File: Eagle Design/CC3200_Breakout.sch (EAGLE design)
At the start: 46 parts, among them J22 M10X2, J23 M10X2, U15 AT25FS010, Y2 32.768KHz, Y3 407MHz

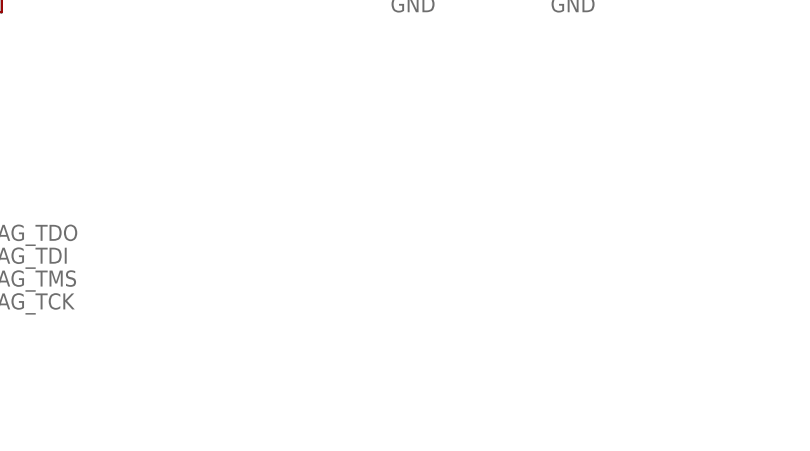
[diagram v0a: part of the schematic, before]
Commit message: Added JTAG and Lock Connectors
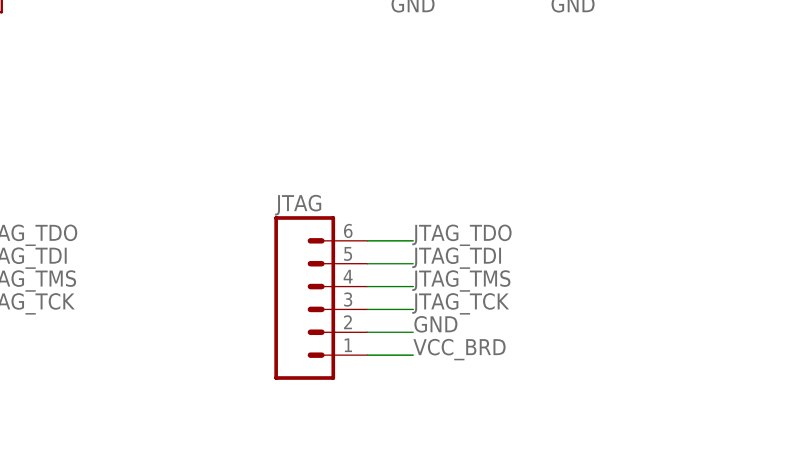
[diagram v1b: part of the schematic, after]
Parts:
- added JTAG: (no value), SparkFun-Connectors:M06SILK_FEMALE_PTH
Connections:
- net GND: now also JTAG.2
- net JTAG_TCK: now also JTAG.3
- net JTAG_TDI: now also JTAG.5
- net JTAG_TDO: now also JTAG.6
- net JTAG_TMS: now also JTAG.4
- net VCC_BRD: now also JTAG.1
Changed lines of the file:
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@@
 <?xml version="1.0" encoding="utf-8"?>
 <!DOCTYPE eagle SYSTEM "eagle.dtd">
-<eagle version="6.4">
+<eagle version="7.1.0">
 <drawing>
 <settings>
@@
 <layers>
 <layer number="1" name="Top" color="4" fill="1" visible="no" active="no"/>
+<layer number="2" name="Route2" color="1" fill="3" visible="no" active="no"/>
+<layer number="3" name="Route3" color="4" fill="3" visible="no" active="no"/>
+<layer number="14" name="Route14" color="1" fill="6" visible="no" active="no"/>
+<layer number="15" name="Route15" color="4" fill="6" visible="no" active="no"/>
 <layer number="16" name="Bottom" color="1" fill="1" visible="no" active="no"/>
 <layer number="17" name="Pads" color="2" fill="1" visible="no" active="no"/>
@@
 <layer number="54" name="bGND_GNDA" color="1" fill="9" visible="no" active="no"/>
 <layer number="56" name="wert" color="7" fill="1" visible="no" active="no"/>
+<layer number="57" name="tCAD" color="7" fill="1" visible="no" active="no"/>
+<layer number="90" name="Modules" color="5" fill="1" visible="yes" active="yes"/>
 <layer number="91" name="Nets" color="2" fill="1" visible="yes" active="yes"/>
 <layer number="92" name="Busses" color="1" fill="1" visible="yes" active="yes"/>
@@
 <layer number="97" name="Info" color="7" fill="1" visible="yes" active="yes"/>
 <layer number="98" name="Guide" color="6" fill="1" visible="yes" active="yes"/>
+<layer number="99" name="SpiceOrder" color="7" fill="1" visible="yes" active="yes"/>
 <layer number="100" name="Muster" color="7" fill="1" visible="no" active="no"/>
 <layer number="101" name="Patch_Top" color="12" fill="4" visible="no" active="yes"/>
@@
 <layer number="108" name="tplace-old" color="10" fill="1" visible="yes" active="yes"/>
 <layer number="109" name="ref-old" color="11" fill="1" visible="yes" active="yes"/>
+<layer number="110" name="fp0" color="7" fill="1" visible="yes" active="yes"/>
+<layer number="111" name="LPC17xx" color="7" fill="1" visible="yes" active="yes"/>
+<layer number="112" name="tSilk" color="7" fill="1" visible="yes" active="yes"/>
+<layer number="113" name="IDFDebug" color="4" fill="1" visible="yes" active="yes"/>
 <layer number="116" name="Patch_BOT" color="9" fill="4" visible="no" active="yes"/>
 <layer number="121" name="_tsilk" color="7" fill="1" visible="no" active="yes"/>
 <layer number="122" name="_bsilk" color="7" fill="1" visible="no" active="yes"/>
+<layer number="123" name="tTestmark" color="7" fill="1" visible="yes" active="yes"/>
+<layer number="124" name="bTestmark" color="7" fill="1" visible="yes" active="yes"/>
 <layer number="125" name="_tNames" color="7" fill="1" visible="no" active="yes"/>
+<layer number="126" name="_bNames" color="7" fill="1" visible="yes" active="yes"/>
+<layer number="127" name="_tValues" color="7" fill="1" visible="yes" active="yes"/>
+<layer number="128" name="_bValues" color="7" fill="1" visible="yes" active="yes"/>
+<layer number="131" name="tAdjust" color="7" fill="1" visible="yes" active="yes"/>
+<layer number="132" name="bAdjust" color="7" fill="1" visible="yes" active="yes"/>
 <layer number="144" name="Drill_legend" color="7" fill="1" visible="no" active="yes"/>
+<layer number="150" name="Notes" color="7" fill="1" visible="yes" active="yes"/>
 <layer number="151" name="HeatSink" color="7" fill="1" visible="no" active="yes"/>
+<layer number="152" name="_bDocu" color="7" fill="1" visible="yes" active="yes"/>
+<layer number="153" name="FabDoc1" color="7" fill="1" visible="yes" active="yes"/>
+<layer number="154" name="FabDoc2" color="7" fill="1" visible="yes" active="yes"/>
+<layer number="155" name="FabDoc3" color="7" fill="1" visible="yes" active="yes"/>
 <layer number="199" name="Contour" color="7" fill="1" visible="no" active="yes"/>
 <layer number="200" name="200bmp" color="1" fill="10" visible="no" active="yes"/>
@@
 <layer number="223" name="223bmp" color="24" fill="1" visible="no" active="no"/>
 <layer number="224" name="224bmp" color="25" fill="1" visible="no" active="no"/>
+<layer number="248" name="Housing" color="7" fill="1" visible="yes" active="yes"/>
+<layer number="249" name="Edge" color="7" fill="1" visible="yes" active="yes"/>
 <layer number="250" name="Descript" color="3" fill="1" visible="no" active="no"/>
 <layer number="251" name="SMDround" color="12" fill="11" visible="no" active="no"/>
@@
 <part name="J22" library="SparkFun-Connectors" deviceset="M10X2" device=""/>
 <part name="J23" library="SparkFun-Connectors" deviceset="M10X2" device=""/>
+<part name="JTAG" library="SparkFun-Connectors" deviceset="M06" device="SILK_FEMALE_PTH"/>
 </parts>
 <sheets>
@@
 <instance part="J22" gate="G$1" x="210.82" y="132.08"/>
 <instance part="J23" gate="G$1" x="271.78" y="132.08"/>
+<instance part="JTAG" gate="G$1" x="193.04" y="25.4"/>
 </instances>
 <busses>
@@
 <label x="154.94" y="33.02" size="1.778" layer="95"/>
 </segment>
+<segment>
+<wire x1="198.12" y1="33.02" x2="203.2" y2="33.02" width="0.1524" layer="91"/>
+<label x="203.2" y="33.02" size="1.778" layer="95"/>
+<pinref part="JTAG" gate="G$1" pin="6"/>
+</segment>
 </net>
 <net name="JTAG_TDI" class="0">
@@
 <label x="154.94" y="30.48" size="1.778" layer="95"/>
 </segment>
+<segment>
+<wire x1="198.12" y1="30.48" x2="203.2" y2="30.48" width="0.1524" layer="91"/>
+<label x="203.2" y="30.48" size="1.778" layer="95"/>
+<pinref part="JTAG" gate="G$1" pin="5"/>
+</segment>
 </net>
 <net name="JTAG_TMS" class="0">
@@
 <label x="154.94" y="27.94" size="1.778" layer="95"/>
 </segment>
+<segment>
+<wire x1="198.12" y1="27.94" x2="203.2" y2="27.94" width="0.1524" layer="91"/>
+<label x="203.2" y="27.94" size="1.778" layer="95"/>
+<pinref part="JTAG" gate="G$1" pin="4"/>
+</segment>
 </net>
 <net name="JTAG_TCK" class="0">
@@
 <wire x1="116.84" y1="25.4" x2="116.84" y2="53.34" width="0.1524" layer="91"/>
 <label x="154.94" y="25.4" size="1.778" layer="95"/>
+</segment>
+<segment>
+<wire x1="198.12" y1="25.4" x2="203.2" y2="25.4" width="0.1524" layer="91"/>
+<label x="203.2" y="25.4" size="1.778" layer="95"/>
+<pinref part="JTAG" gate="G$1" pin="3"/>
 </segment>
 </net>
@@
 <wire x1="289.56" y1="142.24" x2="279.4" y2="142.24" width="0.1524" layer="91"/>
 <label x="289.56" y="142.24" size="1.778" layer="95"/>
+</segment>
+<segment>
+<wire x1="198.12" y1="22.86" x2="203.2" y2="22.86" width="0.1524" layer="91"/>
+<label x="203.2" y="22.86" size="1.778" layer="95"/>
+<pinref part="JTAG" gate="G$1" pin="2"/>
 </segment>
 </net>
@@
 <label x="193.04" y="142.24" size="1.778" layer="95"/>
 </segment>
-</net>
+<segment>
+<pinref part="JTAG" gate="G$1" pin="1"/>
+<wire x1="198.12" y1="20.32" x2="203.2" y2="20.32" width="0.1524" layer="91"/>
+<label x="203.2" y="20.32" size="1.778" layer="95"/>
+</segment>
+</net>

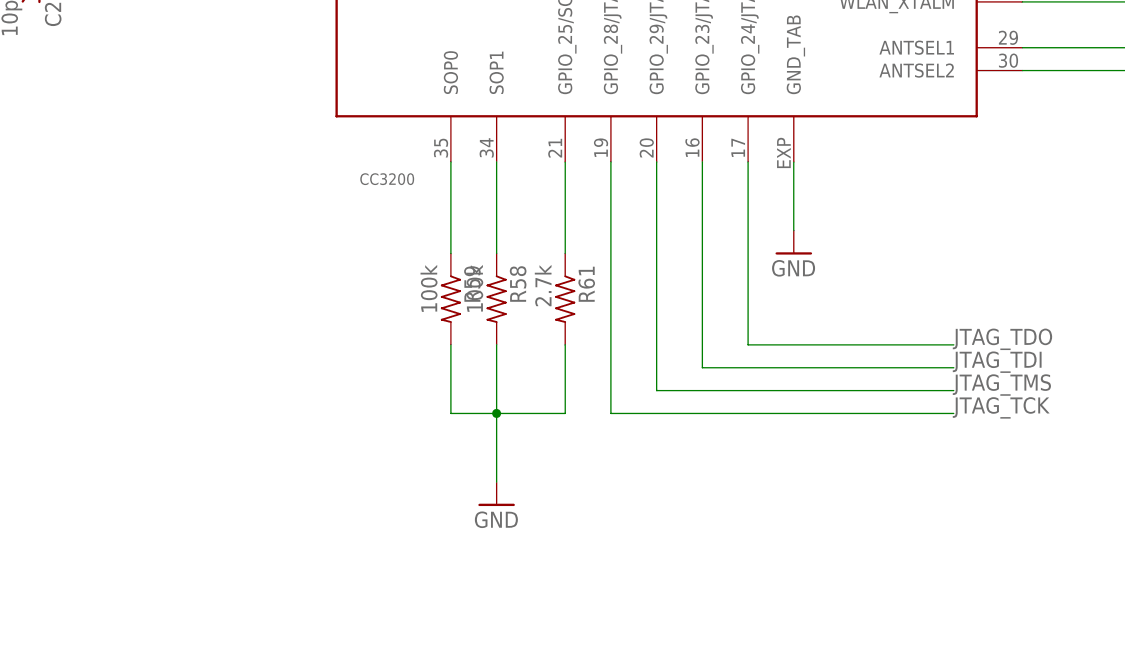
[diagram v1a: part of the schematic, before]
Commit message: SOP
Added SOP connector and addition connector JP90 to be use as jumper wire
used in Energia
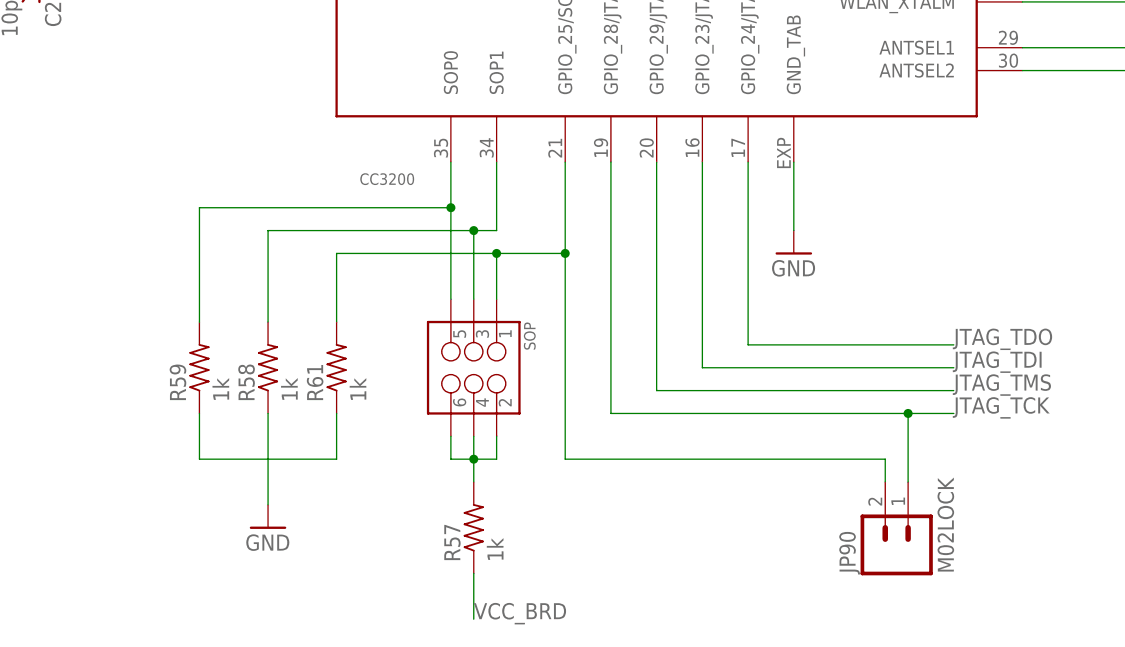
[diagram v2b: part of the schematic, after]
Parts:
- added JP90: M02LOCK, SparkFun-Connectors:M02LOCK
- added R57: 1k, resistor:R-US_R0402
- added SOP: (no value), SparkFun-Connectors:M03X22X3_SILK_MALE_PTH
- R58, R59: value 100k -> 1k
- R61: value 2.7k -> 1k
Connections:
- new net N$6: R57.2, SOP.2, SOP.4, SOP.6
- net GND: now also R58.1, R59.1, R61.1; no longer R58.2, R59.2, R61.2
- net JTAG_TCK: now also JP90.1
- net N$13: now also R59.2, SOP.5; no longer R59.1
- net N$21: now also R58.2, SOP.3; no longer R58.1
- net N$22: now also JP90.2, R61.2, SOP.1; no longer R61.1
- net VCC_BRD: now also R57.1
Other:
- moved on the sheet: R58, R59, R61
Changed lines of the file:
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@@
 <part name="R65" library="resistor" deviceset="R-US_" device="R0402"/>
 <part name="Y2" library="SparkFun-FreqCtrl" deviceset="CRYSTAL" device="5X3" value="32.768KHz"/>
-<part name="R58" library="resistor" deviceset="R-US_" device="R0402" value="100k"/>
-<part name="R61" library="resistor" deviceset="R-US_" device="R0402" value="2.7k"/>
-<part name="R59" library="resistor" deviceset="R-US_" device="R0402" value="100k"/>
-<part name="GND25" library="SparkFun-Aesthetics" deviceset="GND" device=""/>
 <part name="GND23" library="SparkFun-Aesthetics" deviceset="GND" device=""/>
 <part name="GND13" library="SparkFun-Aesthetics" deviceset="GND" device=""/>
@@
 <part name="J23" library="SparkFun-Connectors" deviceset="M10X2" device=""/>
 <part name="JTAG" library="SparkFun-Connectors" deviceset="M06" device="SILK_FEMALE_PTH"/>
+<part name="SOP" library="SparkFun-Connectors" deviceset="M03X2" device="2X3_SILK_MALE_PTH"/>
+<part name="R57" library="resistor" deviceset="R-US_" device="R0402" value="1k"/>
+<part name="JP90" library="SparkFun-Connectors" deviceset="M02" device="LOCK"/>
+<part name="R59" library="resistor" deviceset="R-US_" device="R0402" value="1k"/>
+<part name="R58" library="resistor" deviceset="R-US_" device="R0402" value="1k"/>
+<part name="R61" library="resistor" deviceset="R-US_" device="R0402" value="1k"/>
+<part name="GND25" library="SparkFun-Aesthetics" deviceset="GND" device=""/>
 </parts>
 <sheets>
@@
 <instance part="R65" gate="G$1" x="27.94" y="106.68" rot="R180"/>
 <instance part="Y2" gate="G$1" x="60.96" y="78.74" rot="R90"/>
-<instance part="R58" gate="G$1" x="104.14" y="38.1" rot="R270"/>
-<instance part="R61" gate="G$1" x="111.76" y="38.1" rot="R270"/>
-<instance part="R59" gate="G$1" x="99.06" y="38.1" rot="R270"/>
-<instance part="GND25" gate="1" x="104.14" y="15.24"/>
 <instance part="GND23" gate="1" x="137.16" y="43.18"/>
 <instance part="GND13" gate="1" x="43.18" y="83.82" rot="R270"/>
@@
 <instance part="J23" gate="G$1" x="271.78" y="132.08"/>
 <instance part="JTAG" gate="G$1" x="193.04" y="25.4"/>
+<instance part="SOP" gate="G$1" x="101.6" y="30.48" rot="R270"/>
+<instance part="R57" gate="G$1" x="101.6" y="12.7" rot="R90"/>
+<instance part="JP90" gate="G$1" x="149.86" y="10.16" rot="R90"/>
+<instance part="R59" gate="G$1" x="71.12" y="30.48" rot="R90"/>
+<instance part="R58" gate="G$1" x="78.74" y="30.48" rot="R90"/>
+<instance part="R61" gate="G$1" x="86.36" y="30.48" rot="R90"/>
+<instance part="GND25" gate="1" x="78.74" y="12.7"/>
 </instances>
 <busses>
@@
 <net name="N$13" class="0">
 <segment>
-<pinref part="R59" gate="G$1" pin="1"/>
 <pinref part="U$1" gate="G$1" pin="SOP0"/>
-<wire x1="99.06" y1="43.18" x2="99.06" y2="53.34" width="0.1524" layer="91"/>
+<wire x1="99.06" y1="38.1" x2="99.06" y2="48.26" width="0.1524" layer="91"/>
+<pinref part="SOP" gate="G$1" pin="5"/>
+<pinref part="R59" gate="G$1" pin="2"/>
+<wire x1="99.06" y1="48.26" x2="99.06" y2="53.34" width="0.1524" layer="91"/>
+<wire x1="99.06" y1="48.26" x2="71.12" y2="48.26" width="0.1524" layer="91"/>
+<wire x1="71.12" y1="48.26" x2="71.12" y2="35.56" width="0.1524" layer="91"/>
+<junction x="99.06" y="48.26"/>
 </segment>
 </net>
@@
 <segment>
 <pinref part="U$1" gate="G$1" pin="SOP1"/>
-<pinref part="R58" gate="G$1" pin="1"/>
-<wire x1="104.14" y1="53.34" x2="104.14" y2="43.18" width="0.1524" layer="91"/>
+<wire x1="104.14" y1="53.34" x2="104.14" y2="45.72" width="0.1524" layer="91"/>
+<pinref part="SOP" gate="G$1" pin="3"/>
+<wire x1="104.14" y1="45.72" x2="101.6" y2="45.72" width="0.1524" layer="91"/>
+<wire x1="101.6" y1="45.72" x2="101.6" y2="38.1" width="0.1524" layer="91"/>
+<pinref part="R58" gate="G$1" pin="2"/>
+<wire x1="101.6" y1="45.72" x2="78.74" y2="45.72" width="0.1524" layer="91"/>
+<wire x1="78.74" y1="45.72" x2="78.74" y2="35.56" width="0.1524" layer="91"/>
+<junction x="101.6" y="45.72"/>
 </segment>
 </net>
@@
 <segment>
 <pinref part="U$1" gate="G$1" pin="GPIO_25/SOP2"/>
-<pinref part="R61" gate="G$1" pin="1"/>
 <wire x1="111.76" y1="53.34" x2="111.76" y2="43.18" width="0.1524" layer="91"/>
+<pinref part="JP90" gate="G$1" pin="2"/>
+<wire x1="111.76" y1="43.18" x2="111.76" y2="20.32" width="0.1524" layer="91"/>
+<wire x1="111.76" y1="20.32" x2="147.32" y2="20.32" width="0.1524" layer="91"/>
+<wire x1="147.32" y1="20.32" x2="147.32" y2="17.78" width="0.1524" layer="91"/>
+<pinref part="SOP" gate="G$1" pin="1"/>
+<wire x1="111.76" y1="43.18" x2="104.14" y2="43.18" width="0.1524" layer="91"/>
+<wire x1="104.14" y1="43.18" x2="104.14" y2="38.1" width="0.1524" layer="91"/>
+<pinref part="R61" gate="G$1" pin="2"/>
+<wire x1="104.14" y1="43.18" x2="86.36" y2="43.18" width="0.1524" layer="91"/>
+<wire x1="86.36" y1="43.18" x2="86.36" y2="35.56" width="0.1524" layer="91"/>
+<junction x="104.14" y="43.18"/>
+<junction x="111.76" y="43.18"/>
 </segment>
 </net>
@@
 <segment>
 <pinref part="U$1" gate="G$1" pin="GPIO_28/JTAG_TCK"/>
-<wire x1="154.94" y1="25.4" x2="116.84" y2="25.4" width="0.1524" layer="91"/>
+<wire x1="154.94" y1="25.4" x2="149.86" y2="25.4" width="0.1524" layer="91"/>
+<wire x1="149.86" y1="25.4" x2="116.84" y2="25.4" width="0.1524" layer="91"/>
 <wire x1="116.84" y1="25.4" x2="116.84" y2="53.34" width="0.1524" layer="91"/>
 <label x="154.94" y="25.4" size="1.778" layer="95"/>
+<pinref part="JP90" gate="G$1" pin="1"/>
+<wire x1="149.86" y1="17.78" x2="149.86" y2="25.4" width="0.1524" layer="91"/>
+<junction x="149.86" y="25.4"/>
 </segment>
 <segment>
@@
 </net>
 <net name="GND" class="0">
-<segment>
-<pinref part="R59" gate="G$1" pin="2"/>
-<wire x1="99.06" y1="33.02" x2="99.06" y2="25.4" width="0.1524" layer="91"/>
-<pinref part="R61" gate="G$1" pin="2"/>
-<wire x1="99.06" y1="25.4" x2="104.14" y2="25.4" width="0.1524" layer="91"/>
-<wire x1="104.14" y1="25.4" x2="111.76" y2="25.4" width="0.1524" layer="91"/>
-<wire x1="111.76" y1="25.4" x2="111.76" y2="33.02" width="0.1524" layer="91"/>
-<pinref part="R58" gate="G$1" pin="2"/>
-<wire x1="104.14" y1="33.02" x2="104.14" y2="25.4" width="0.1524" layer="91"/>
-<junction x="104.14" y="25.4"/>
-<wire x1="104.14" y1="25.4" x2="104.14" y2="17.78" width="0.1524" layer="91"/>
-<pinref part="GND25" gate="1" pin="GND"/>
-</segment>
 <segment>
 <pinref part="U$1" gate="G$1" pin="GND_TAB"/>
@@
 <label x="203.2" y="22.86" size="1.778" layer="95"/>
 <pinref part="JTAG" gate="G$1" pin="2"/>
+</segment>
+<segment>
+<pinref part="R59" gate="G$1" pin="1"/>
+<wire x1="71.12" y1="25.4" x2="71.12" y2="20.32" width="0.1524" layer="91"/>
+<pinref part="R61" gate="G$1" pin="1"/>
+<wire x1="71.12" y1="20.32" x2="78.74" y2="20.32" width="0.1524" layer="91"/>
+<wire x1="78.74" y1="20.32" x2="86.36" y2="20.32" width="0.1524" layer="91"/>
+<wire x1="86.36" y1="20.32" x2="86.36" y2="25.4" width="0.1524" layer="91"/>
+<pinref part="R58" gate="G$1" pin="1"/>
+<wire x1="78.74" y1="25.4" x2="78.74" y2="20.32" width="0.1524" layer="91"/>
+<wire x1="78.74" y1="20.32" x2="78.74" y2="15.24" width="0.1524" layer="91"/>
+<pinref part="GND25" gate="1" pin="GND"/>
 </segment>
 </net>
@@
 <label x="203.2" y="20.32" size="1.778" layer="95"/>
 </segment>
+<segment>
+<pinref part="R57" gate="G$1" pin="1"/>
+<wire x1="101.6" y1="7.62" x2="101.6" y2="2.54" width="0.1524" layer="91"/>
+<label x="101.6" y="2.54" size="1.778" layer="95"/>
+</segment>
 </net>
 <net name="58" class="0">
@@
 </segment>
 </net>
+<net name="N$6" class="0">
+<segment>
+<pinref part="SOP" gate="G$1" pin="6"/>
+<wire x1="99.06" y1="22.86" x2="99.06" y2="20.32" width="0.1524" layer="91"/>
+<wire x1="99.06" y1="20.32" x2="101.6" y2="20.32" width="0.1524" layer="91"/>
+<pinref part="SOP" gate="G$1" pin="4"/>
+<wire x1="101.6" y1="22.86" x2="101.6" y2="20.32" width="0.1524" layer="91"/>
+<wire x1="101.6" y1="20.32" x2="104.14" y2="20.32" width="0.1524" layer="91"/>
+<pinref part="SOP" gate="G$1" pin="2"/>
+<wire x1="104.14" y1="20.32" x2="104.14" y2="22.86" width="0.1524" layer="91"/>
+<junction x="101.6" y="20.32"/>
+<wire x1="101.6" y1="20.32" x2="101.6" y2="17.78" width="0.1524" layer="91"/>
+<pinref part="R57" gate="G$1" pin="2"/>
+</segment>
+</net>
